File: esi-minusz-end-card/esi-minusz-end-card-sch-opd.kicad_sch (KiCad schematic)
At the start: 59 parts, among them Q1 DMP2240UDM, Q2 PMV45EN, Q3 PMV45EN, Q4 PMV45EN, Q5 DMP2240UDM-7, Q6 PMV45EN, Q7 DMP2240UDM-7, U11 MIC842LYC5, U12 MIC842LYC5, U2 MAX7310, U201 TS5A21366, U202 TS5A21366, U203 TS5A21366, U204 TS5A21366

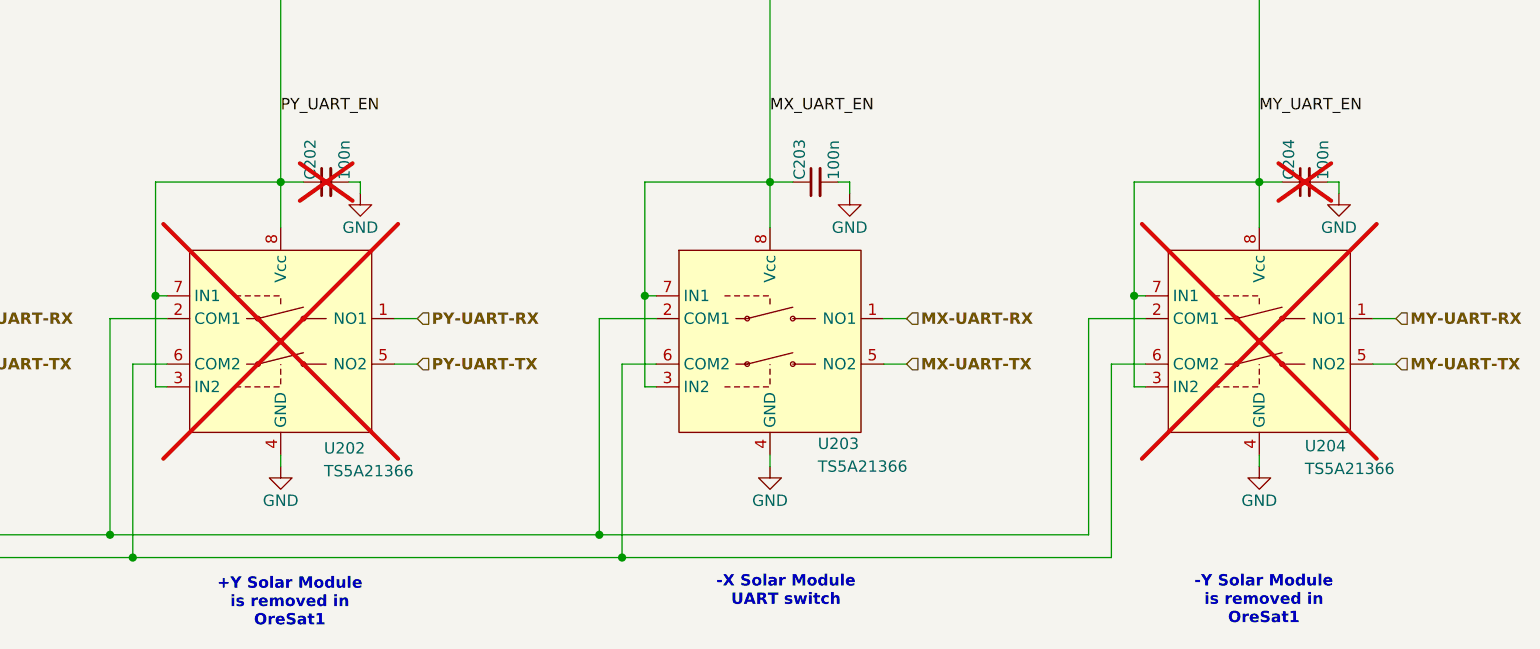
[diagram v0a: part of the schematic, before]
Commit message: Finalized dipole changes, added -/+ Y solar mods. Believe this is finished
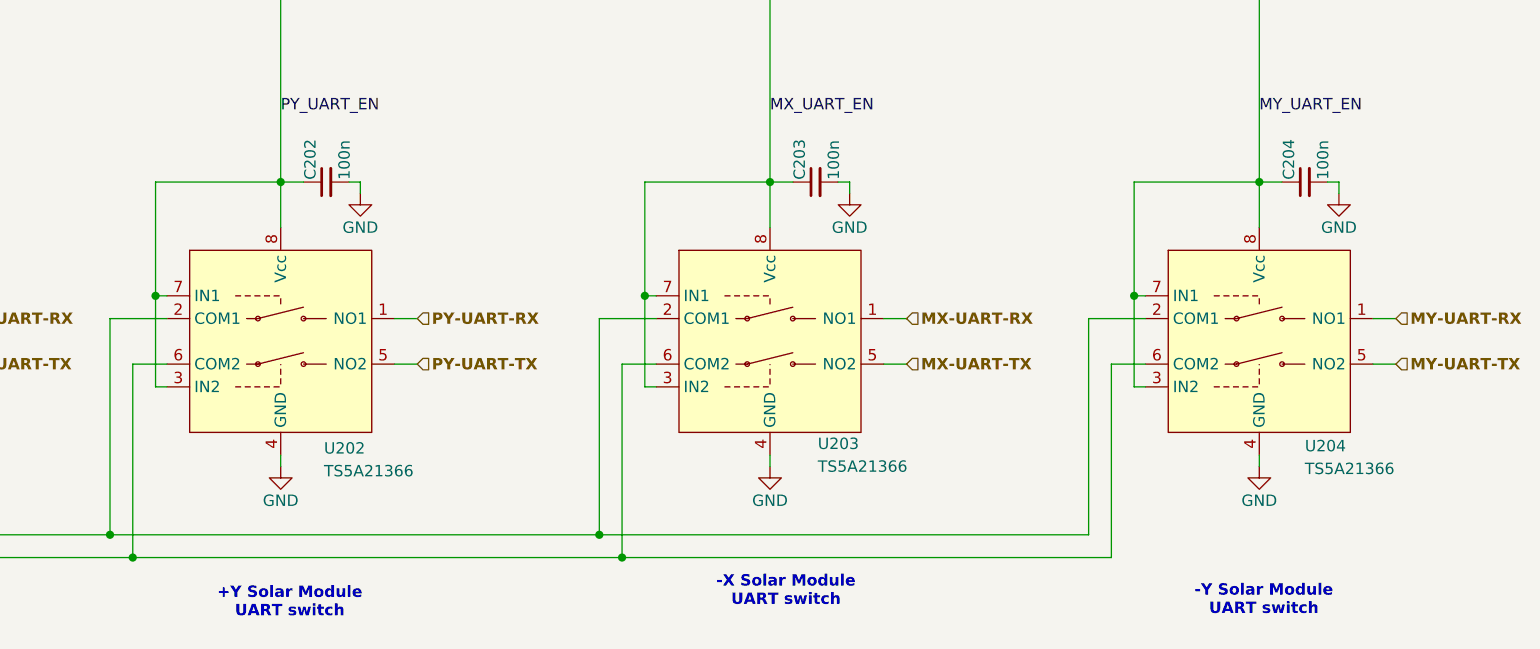
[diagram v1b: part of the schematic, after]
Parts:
- C202, C204, U202, U204: now fitted
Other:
- note added: "+Y Solar Module UART switch"
- note added: "-Y Solar Module UART switch"
- note removed: "+Y Solar Module is removed in OreSat1"
- note removed: "-Y Solar Module is removed in OreSat1"
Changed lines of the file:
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@@
 		(company "Portland State Aerospace Society")
 	)
-	(text "-Y Solar Module \nis removed in \nOreSat1"
+	(text "-Y Solar Module \nUART switch"
 		(exclude_from_sim no)
 		(at 324.358 223.266 0)
@@
 		)
 	)
-	(text "+Y Solar Module \nis removed in \nOreSat1"
+	(text "+Y Solar Module \nUART switch\n"
 		(exclude_from_sim no)
 		(at 215.646 223.52 0)
@@
 		(in_bom yes)
 		(on_board yes)
-		(dnp yes)
+		(dnp no)
 		(property "Reference" "U202"
 			(at 219.456 206.248 0)
@@
 		(in_bom yes)
 		(on_board yes)
-		(dnp yes)
+		(dnp no)
 		(property "Reference" "U204"
 			(at 328.93 205.994 0)
@@
 		(in_bom yes)
 		(on_board yes)
-		(dnp yes)
+		(dnp no)
 		(property "Reference" "C204"
 			(at 327.152 176.276 0)
@@
 		(in_bom yes)
 		(on_board yes)
-		(dnp yes)
+		(dnp no)
 		(property "Reference" "C202"
 			(at 217.932 176.276 0)

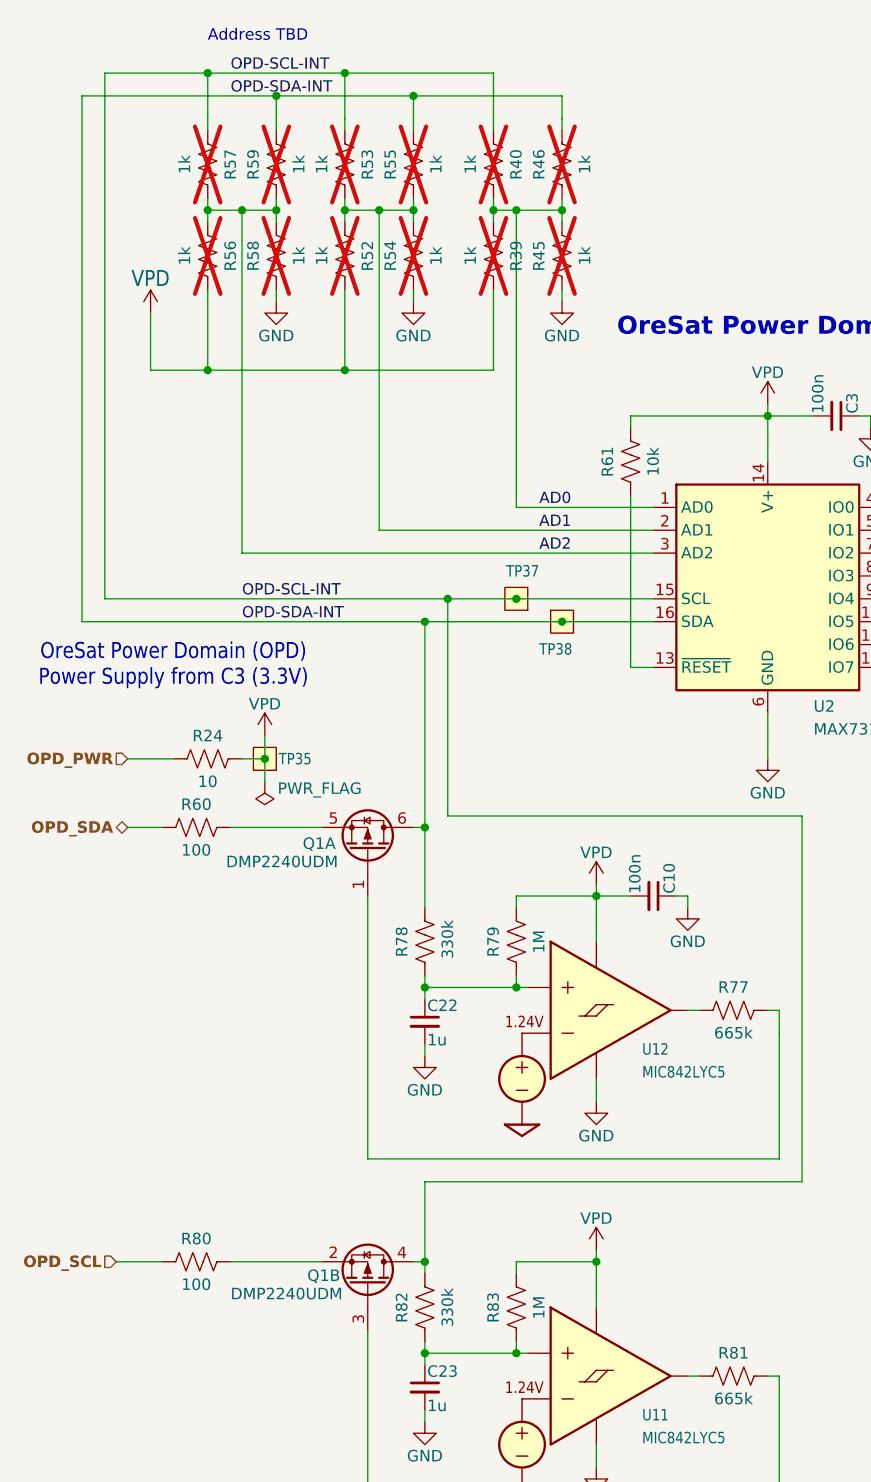
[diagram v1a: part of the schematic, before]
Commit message: ESI v1.0 -Z End Card for fab
Added makefile and readme, fixed BOM error, moved to better RF zone rules
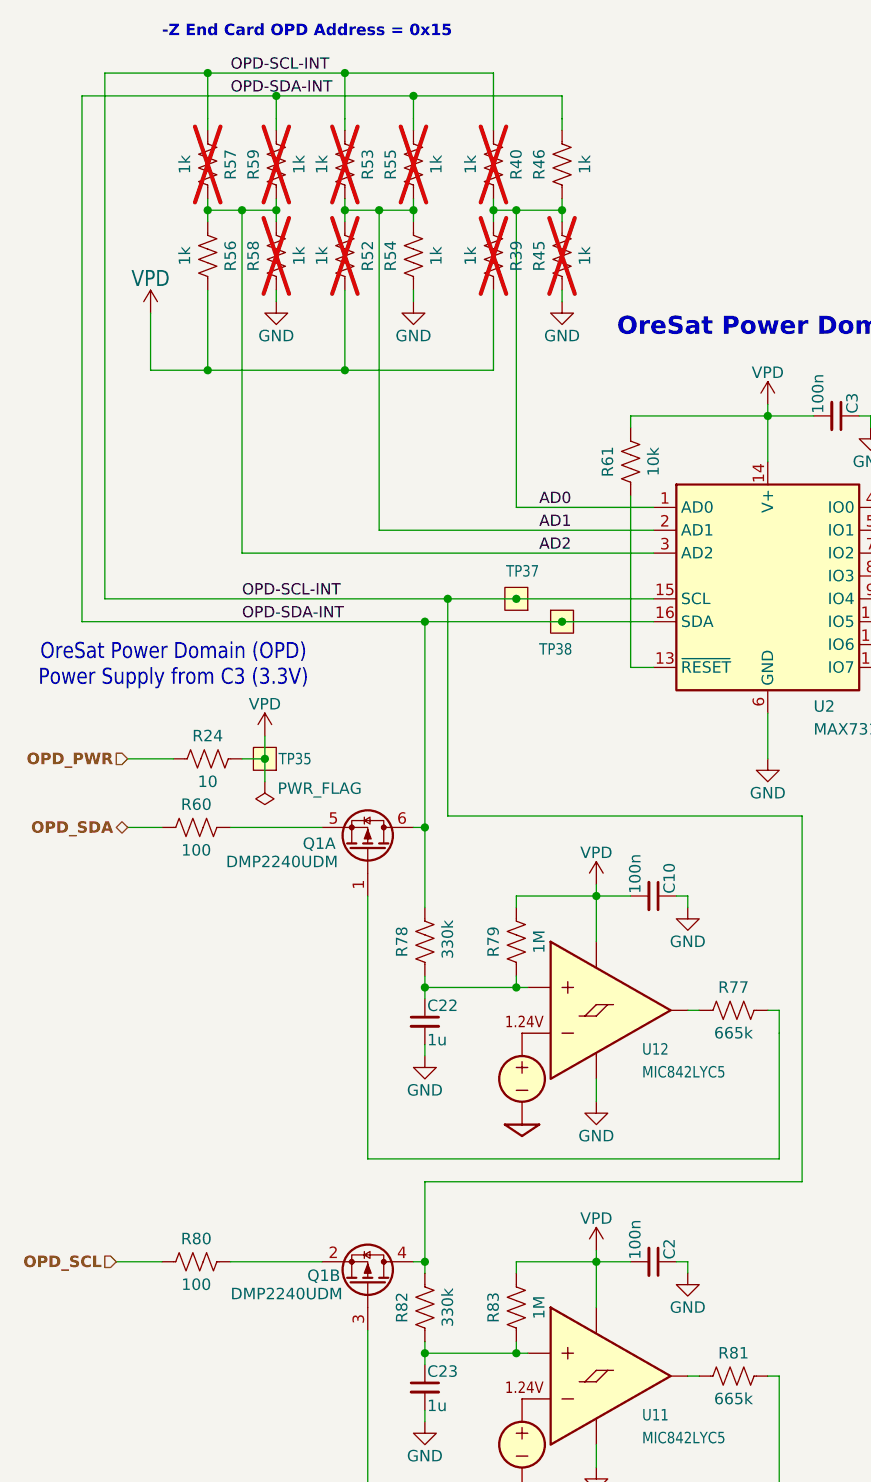
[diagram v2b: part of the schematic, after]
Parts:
- added C2: 100n, oresat-passives:0603-C-NOSILK, symbol Device:C_Small
- Q1, Q5, Q7: MPN DMP2240UDM -> DMP2240UDM-7
- Q2, Q3, Q4, Q6: DIS Digi-Key -> DigiKey; DPN 1727-2307-1-ND -> 31-DMN3028LQ-7CT-ND; MFR Nexperia -> Diodes Incorporated; MPN PMV45EN2R -> DMN3028LQ-7
- R46, R54, R56: now fitted
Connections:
- net GND: now also C2.1
- net VPD: now also C2.2
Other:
- note added: "-Z End Card OPD Address = 0x15"
- note removed: "Address TBD"
- title: OreSat1 -Z End Card -> ESI -Z End Card
